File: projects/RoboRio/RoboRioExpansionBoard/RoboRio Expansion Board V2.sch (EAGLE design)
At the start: 126 parts, among them J1 RRINTERFACE-FEMALE, J10 SPI_MISO, J11 SPI_MOSI, J12 I2C_SCL, J13 I2C_SDA, J14 UART_TX, J15 UART_RX, J16 LCD, J2 MICROSD-HINGED, J24 TP_GND, J25 PWM0, J26 PWM1, J27 PWM2, J28 PWM3, J29 PWM4, J3 51387-0578, J30 PWM5, J31 PWM6, J32 PWM7, J33 PWM8, J34 PWM9, J35 AI0, J36 AI1, J37 AI2, J38 AI3, J39 AO0, J40 AO1, J8 SPI_CS, J9 SPI_CLK, Q1 NPN-SOT416, Q2 NPN-SOT416, Q3 NPN-SOT416, U1 P8X32A-Q44_P, U2 24LC256ST, U3 FT232RL, U4 TC54VN43, U5 TPS2115APWR, U6 REG1117, U7 ADC124S01, U8 ADC124S01, Y1 5MHz

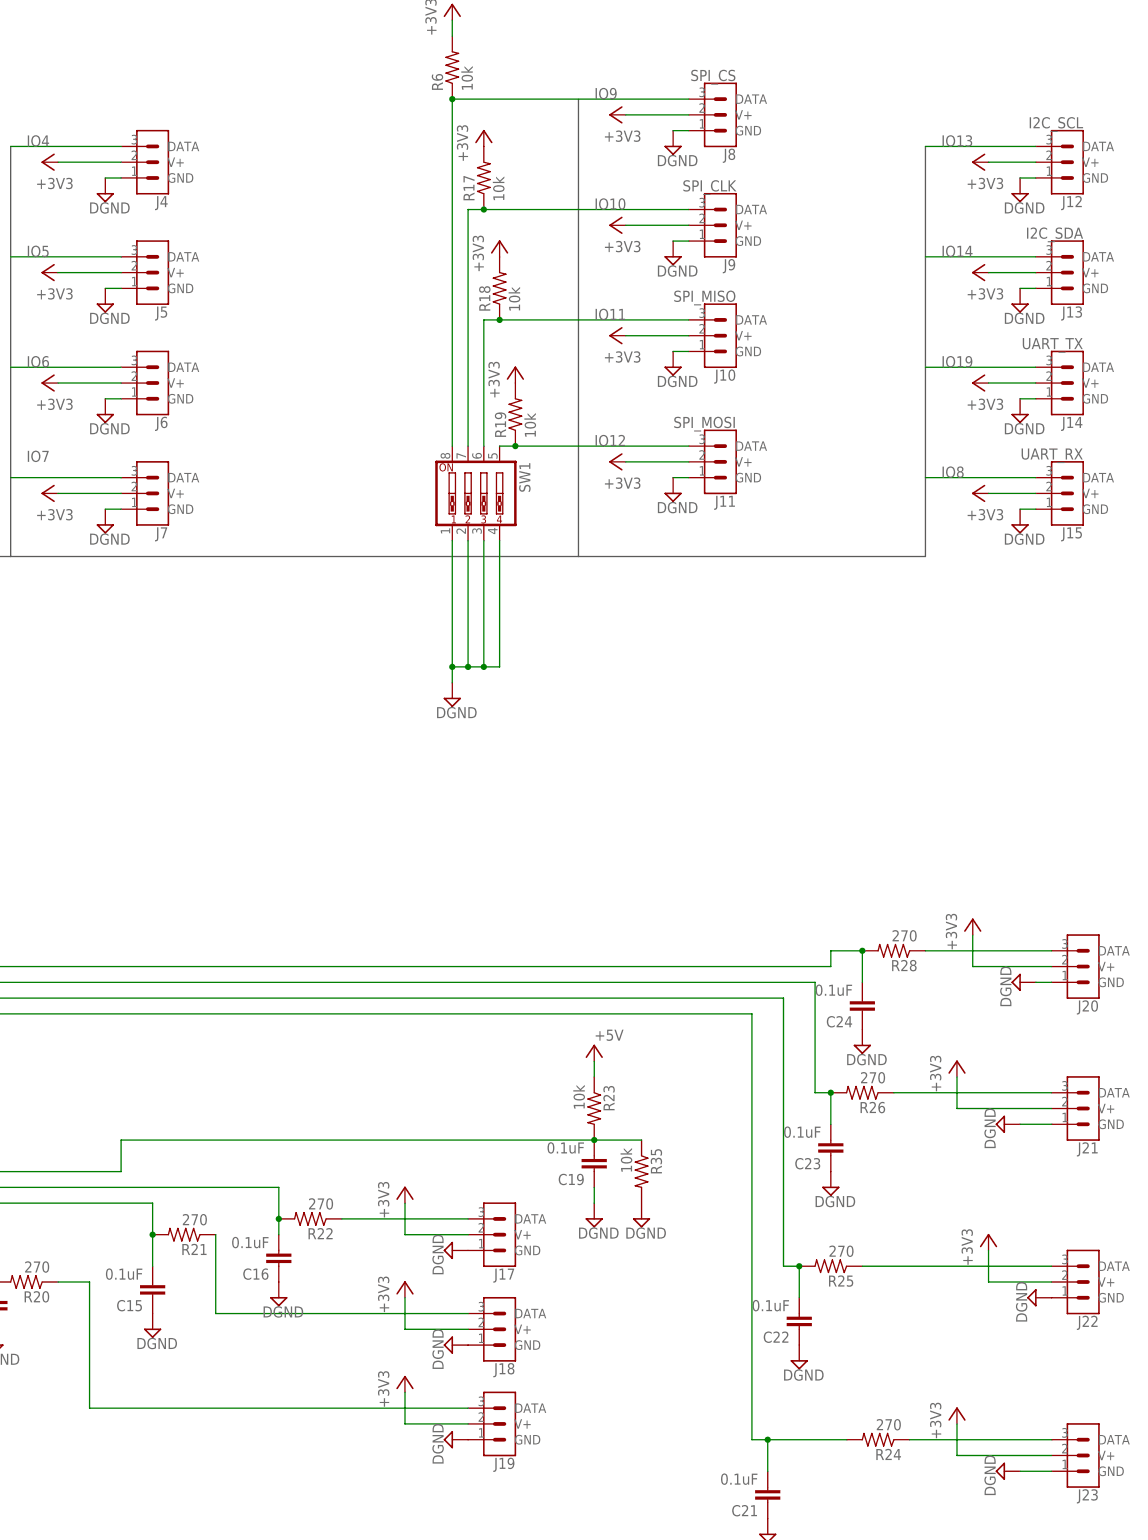
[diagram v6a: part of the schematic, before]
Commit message: Labeled 3 pin connectors
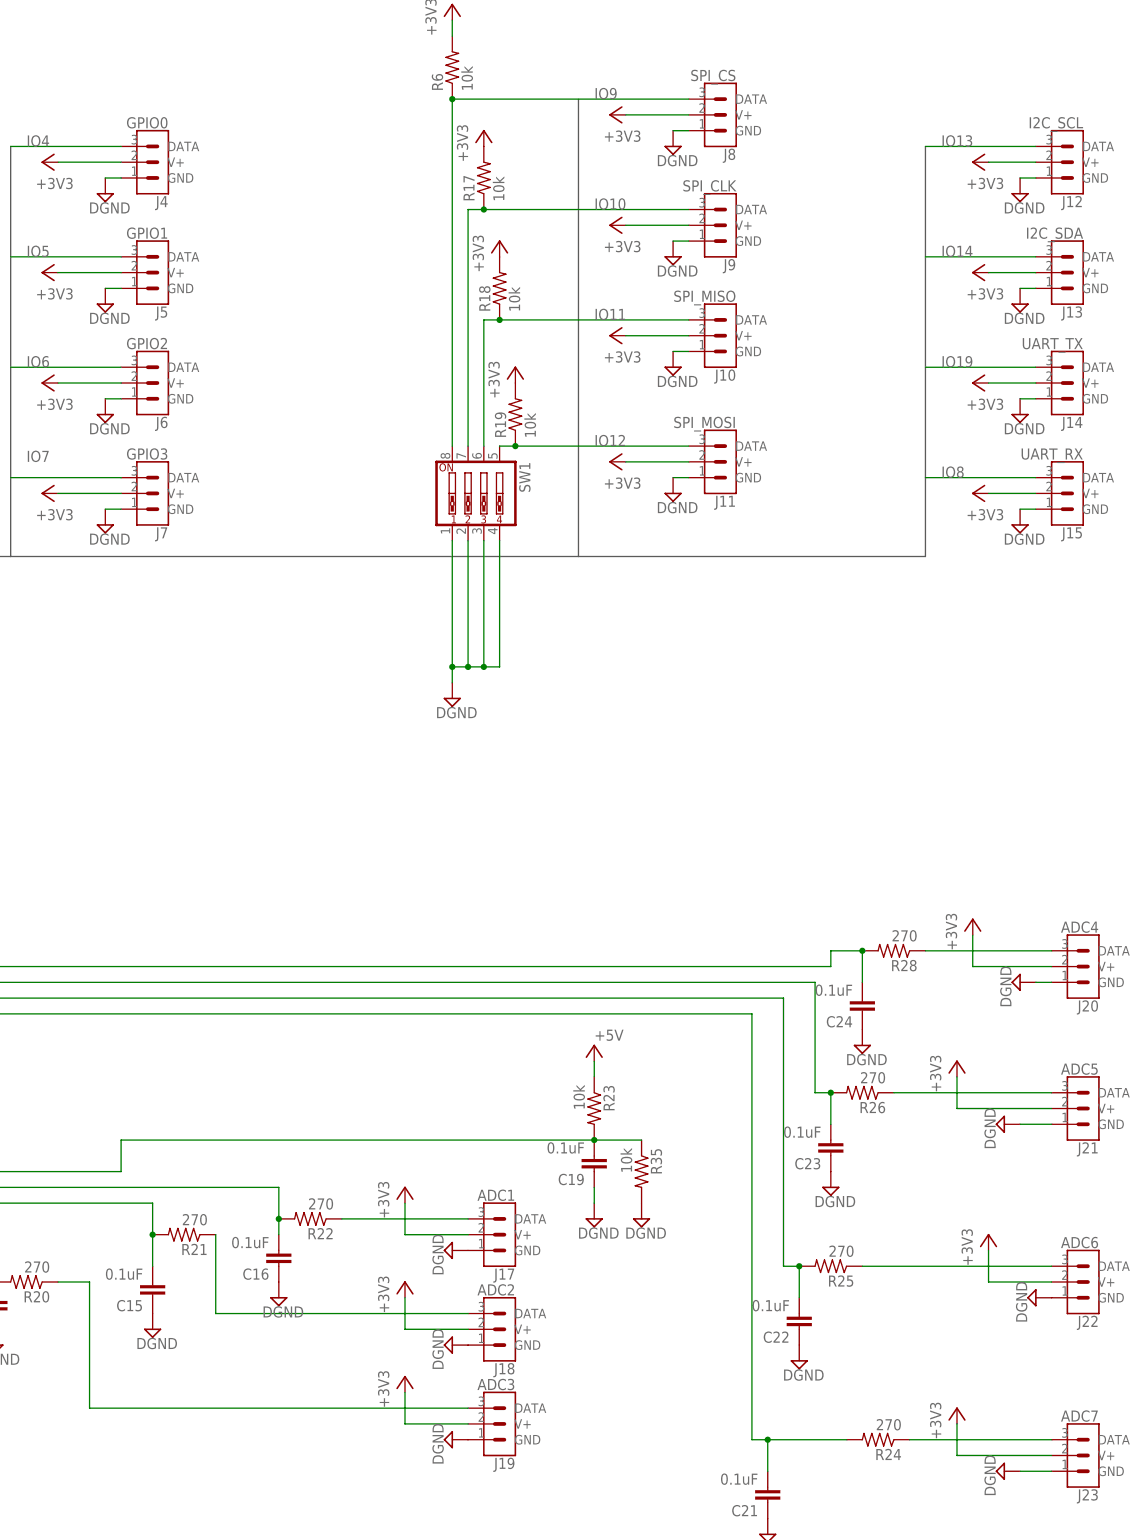
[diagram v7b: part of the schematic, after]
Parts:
- J17: value (none) -> ADC1
- J18: value (none) -> ADC2
- J19: value (none) -> ADC3
- J20: value (none) -> ADC4
- J21: value (none) -> ADC5
- J22: value (none) -> ADC6
- J23: value (none) -> ADC7
- J4: value (none) -> GPIO0
- J5: value (none) -> GPIO1
- J6: value (none) -> GPIO2
- J7: value (none) -> GPIO3
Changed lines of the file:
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@@
 <part name="J40" library="3pin" deviceset="3PINDEVICE" device="DEFAULT" value="AO1"/>
 <part name="SUPPLY30" library="supply2" deviceset="DGND" device=""/>
-<part name="J17" library="3pin" deviceset="3PINDEVICE" device="DEFAULT"/>
-<part name="J18" library="3pin" deviceset="3PINDEVICE" device="DEFAULT"/>
-<part name="J19" library="3pin" deviceset="3PINDEVICE" device="DEFAULT"/>
-<part name="J20" library="3pin" deviceset="3PINDEVICE" device="DEFAULT"/>
-<part name="J21" library="3pin" deviceset="3PINDEVICE" device="DEFAULT"/>
-<part name="J22" library="3pin" deviceset="3PINDEVICE" device="DEFAULT"/>
-<part name="J23" library="3pin" deviceset="3PINDEVICE" device="DEFAULT"/>
+<part name="J17" library="3pin" deviceset="3PINDEVICE" device="DEFAULT" value="ADC1"/>
+<part name="J18" library="3pin" deviceset="3PINDEVICE" device="DEFAULT" value="ADC2"/>
+<part name="J19" library="3pin" deviceset="3PINDEVICE" device="DEFAULT" value="ADC3"/>
+<part name="J20" library="3pin" deviceset="3PINDEVICE" device="DEFAULT" value="ADC4"/>
+<part name="J21" library="3pin" deviceset="3PINDEVICE" device="DEFAULT" value="ADC5"/>
+<part name="J22" library="3pin" deviceset="3PINDEVICE" device="DEFAULT" value="ADC6"/>
+<part name="J23" library="3pin" deviceset="3PINDEVICE" device="DEFAULT" value="ADC7"/>
 <part name="J14" library="3pin" deviceset="3PINDEVICE" device="DEFAULT" value="UART_TX"/>
-<part name="J6" library="3pin" deviceset="3PINDEVICE" device="DEFAULT"/>
-<part name="J5" library="3pin" deviceset="3PINDEVICE" device="DEFAULT"/>
-<part name="J4" library="3pin" deviceset="3PINDEVICE" device="DEFAULT"/>
-<part name="J7" library="3pin" deviceset="3PINDEVICE" device="DEFAULT"/>
+<part name="J6" library="3pin" deviceset="3PINDEVICE" device="DEFAULT" value="GPIO2"/>
+<part name="J5" library="3pin" deviceset="3PINDEVICE" device="DEFAULT" value="GPIO1"/>
+<part name="J4" library="3pin" deviceset="3PINDEVICE" device="DEFAULT" value="GPIO0"/>
+<part name="J7" library="3pin" deviceset="3PINDEVICE" device="DEFAULT" value="GPIO3"/>
 <part name="J15" library="3pin" deviceset="3PINDEVICE" device="DEFAULT" value="UART_RX"/>
 <part name="J8" library="3pin" deviceset="3PINDEVICE" device="DEFAULT" value="SPI_CS"/>
